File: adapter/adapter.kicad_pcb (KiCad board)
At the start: 2 copper layers, 93.5 x 50.9 mm, 27 parts, among them J1 DF3A-2P-2DSA, J10 Ribbon, J11 Ribbon, J12 Ribbon, J9 Ribbon, SW1 CAS-120TA, U1 nice_nano, U2 nice_nano

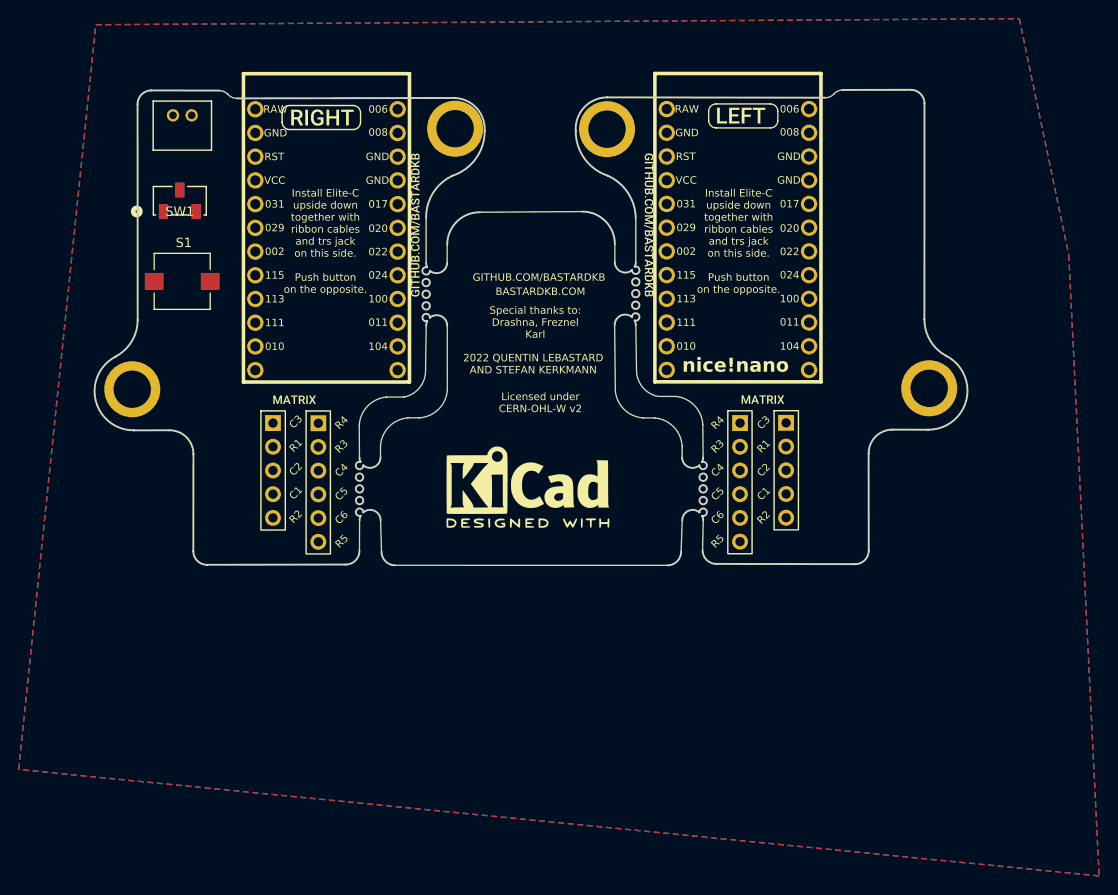
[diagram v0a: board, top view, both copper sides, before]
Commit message: Fix all the pcb routes
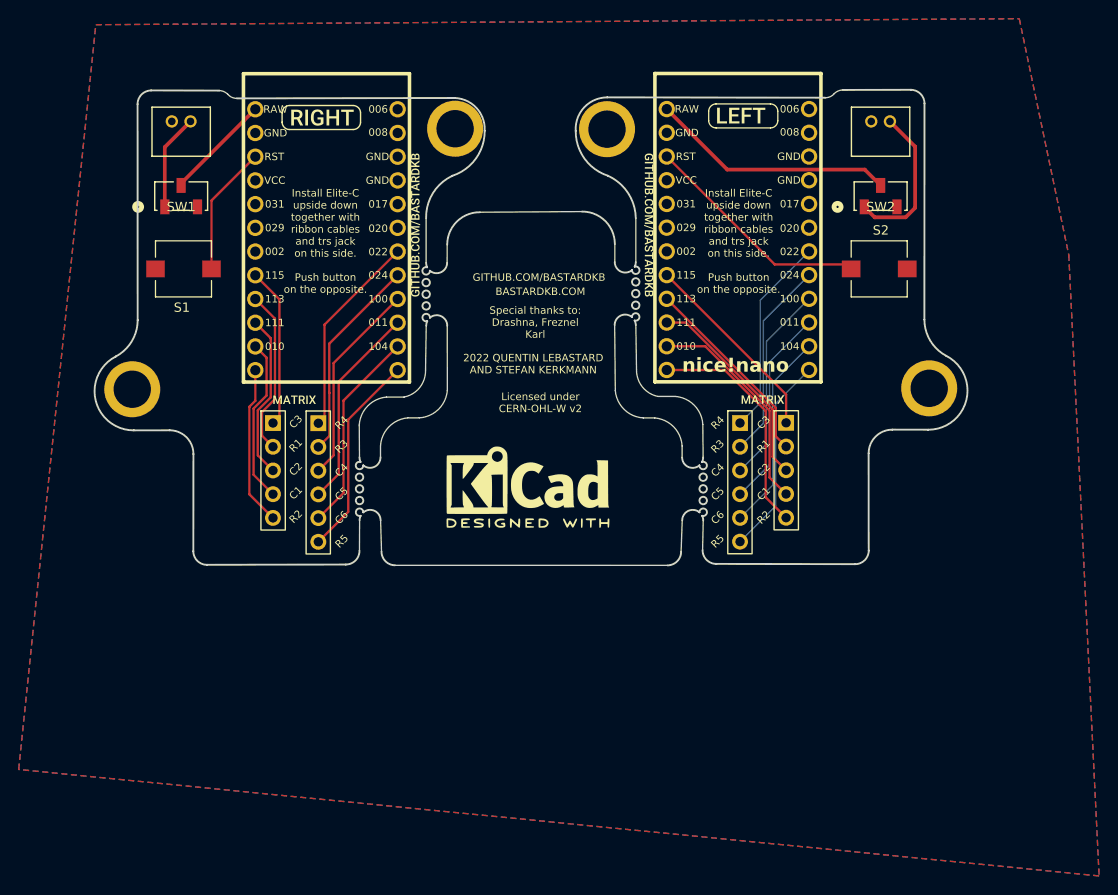
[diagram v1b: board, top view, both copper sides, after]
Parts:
- added J2: DF3A-2P-2DSA, Library:DF3A_2P_2DSA, F.Cu at (191.9, 70.5)
- added S2: TL9210AF180Q, Library:SW_TL9210AF180Q, F.Cu at (192.8, 86.3)
- added SW2: CAS-120TA, Library:CAS-120A_NDC, F.Cu at (192.9, 78.5)
- moved S1 1.34 mm to (118.2, 86.3), turned to 180 degrees
- moved J1 0.66 mm to (117.0, 70.5)
- moved SW1 0.51 mm to (118.0, 78.5)
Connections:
- J1 pad 2: BAT+ -> bat_l
- S1 pad 1: unconnected-(S1-Pad1) -> rst_l
- S1 pad 2: unconnected-(S1-Pad2) -> GND
- SW1 pad 1: unconnected-(SW1-Pad1) -> bat_l
- SW1 pad 2: unconnected-(SW1-Pad2) -> bat_sw_l
- U1 pad 10: unconnected-(U1-P0.11-Pad10) -> col5_l
- U1 pad 11: unconnected-(U1-P1.04-Pad11) -> col6_l
- U1 pad 12: unconnected-(U1-P1.06-Pad12) -> row5_l
- U1 pad 13: unconnected-(U1-NFC1/P0.09-Pad13) -> row2_l
- U1 pad 14: unconnected-(U1-NFC2/P0.10-Pad14) -> col1_l
- U1 pad 15: unconnected-(U1-P1.11-Pad15) -> col2_l
- U1 pad 16: unconnected-(U1-P1.13-Pad16) -> row1_l
- U1 pad 17: unconnected-(U1-P1.15-Pad17) -> col3_l
- U1 pad 22: RST -> rst_l
- U1 pad 24: BAT+ -> bat_sw_l
- U1 pad 3: unconnected-(U1-GND-Pad3) -> GND
- U1 pad 4: unconnected-(U1-GND-Pad4) -> GND
- U1 pad 7: unconnected-(U1-P0.22-Pad7) -> row4_l
- U1 pad 8: unconnected-(U1-P0.24-Pad8) -> row3_l
- U1 pad 9: unconnected-(U1-P1.00-Pad9) -> col4_l
- U2 pad 10: unconnected-(U2-P0.11-Pad10) -> col5_r
- U2 pad 11: unconnected-(U2-P1.04-Pad11) -> col6_r
- U2 pad 12: unconnected-(U2-P1.06-Pad12) -> row5_r
- U2 pad 13: unconnected-(U2-NFC1/P0.09-Pad13) -> row2_r
- U2 pad 14: unconnected-(U2-NFC2/P0.10-Pad14) -> col1_r
- U2 pad 15: unconnected-(U2-P1.11-Pad15) -> col2_r
- U2 pad 16: unconnected-(U2-P1.13-Pad16) -> row1_r
- U2 pad 17: unconnected-(U2-P1.15-Pad17) -> col3_r
- U2 pad 22: unconnected-(U2-RST-Pad22) -> rst_r
- U2 pad 23: unconnected-(U2-GND-Pad23) -> GND
- U2 pad 24: unconnected-(U2-BATIN/P0.04-Pad24) -> bat_sw_r
- U2 pad 3: unconnected-(U2-GND-Pad3) -> GND
- U2 pad 4: unconnected-(U2-GND-Pad4) -> GND
- U2 pad 7: unconnected-(U2-P0.22-Pad7) -> row4_r
- U2 pad 8: unconnected-(U2-P0.24-Pad8) -> row3_r
- U2 pad 9: unconnected-(U2-P1.00-Pad9) -> col4_r
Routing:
- net bat_sw_r: track 0.00 -> 26.3 mm
- net row2_r: track 0.00 -> 24.7 mm
- net rst_r: track 0.00 -> 24.7 mm
- net col1_r: track 0.00 -> 23.5 mm
- net row4_r: track 0.00 -> 22.4 mm
- net col2_r: track 0.00 -> 22.3 mm
- net row3_l: track 0.00 -> 21.9 mm
- net col6_l: track 0.00 -> 21.9 mm
- net row4_l: track 0.00 -> 21.9 mm
- net col5_l: track 0.00 -> 21.9 mm
- net col4_l: track 0.00 -> 21.9 mm
- net row5_l: track 0.00 -> 21.9 mm
- net row3_r: track 0.00 -> 21.4 mm
- net row5_r: track 0.00 -> 21.4 mm
- net col6_r: track 0.00 -> 21.4 mm
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
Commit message: Fix routes in pcb view
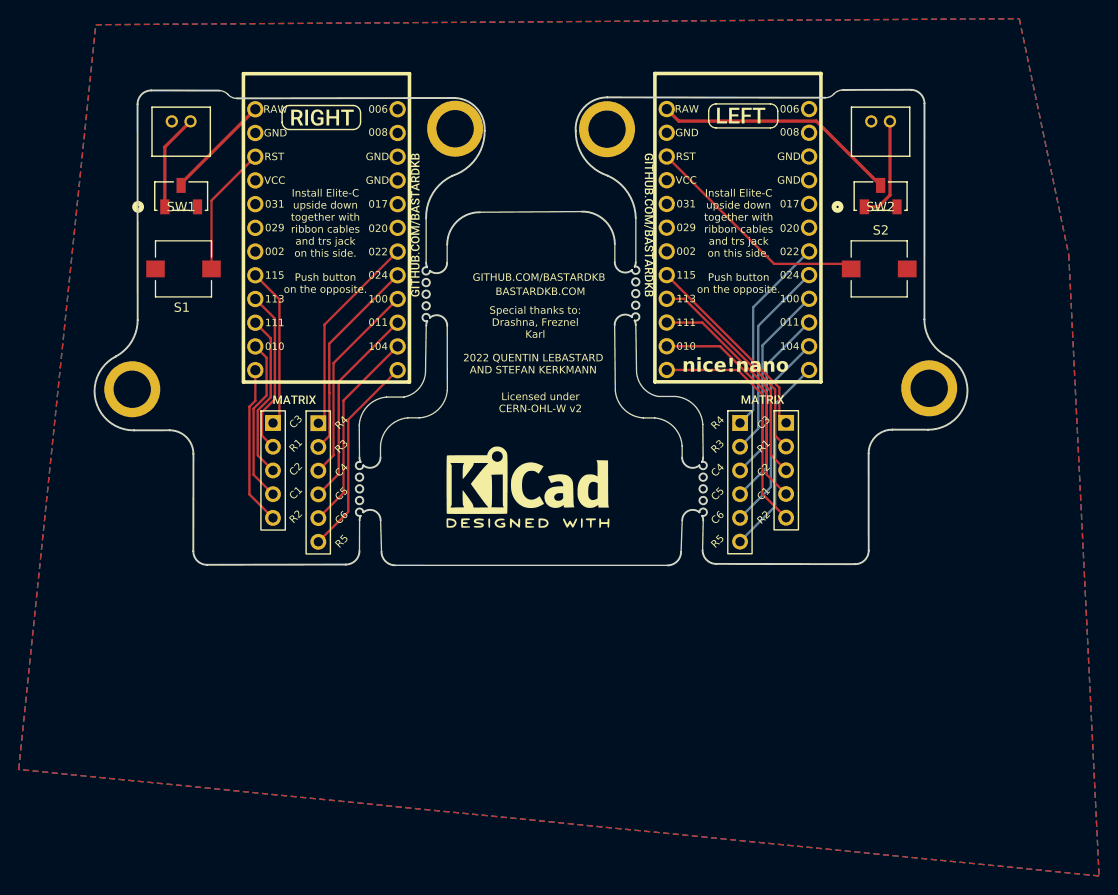
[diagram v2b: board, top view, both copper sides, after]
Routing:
- net bat_r: track 16.7 -> 11.2 mm
- net row1_r: track 21.1 -> 22.2 mm
- net col2_r: track 22.3 -> 23.3 mm
- net col1_r: track 23.5 -> 24.5 mm
- net row2_r: track 24.7 -> 25.6 mm
- net rst_r: track 24.7 -> 25.4 mm
